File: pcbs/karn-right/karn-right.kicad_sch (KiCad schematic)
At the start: 45 parts, among them J1 S2B-PH-K-SLFSN, SW11 SW_Push, SW12 SW_Push, SW13 SW_Push, SW14 SW_Push, SW15 SW_Push, SW21 SW_Push, SW22 SW_Push, SW23 SW_Push, SW24 SW_Push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

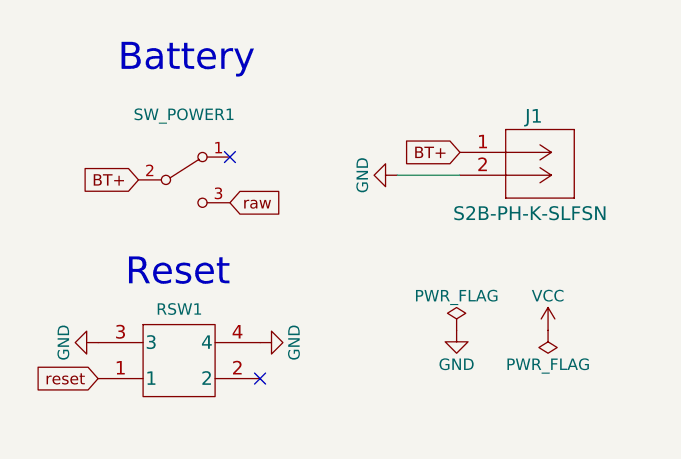
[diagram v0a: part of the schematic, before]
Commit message: Update karn-left pcb
- Apply various fixes from lessons learned on karn-right
- Fix incorrectly oriented reset switch
- Swap incorrect default polarity of JST connector footprint
- Increase size of diode pads
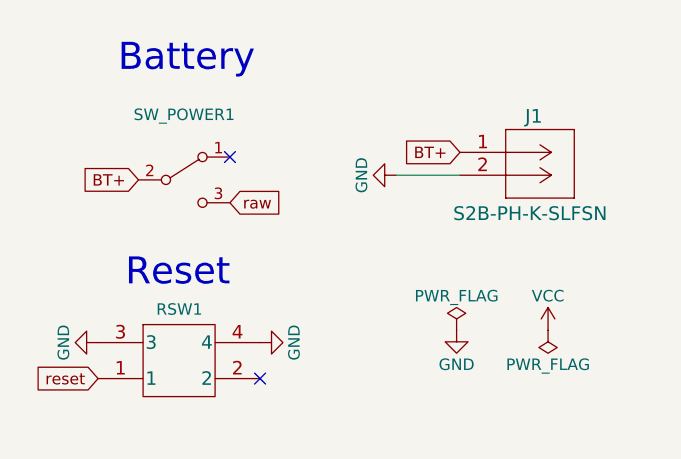
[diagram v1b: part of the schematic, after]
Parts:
- J1: footprint kbd:S2B-PH-K-SLFSN -> CONN_S2B-PH-K-S_JST; symbol S2B-PH-K-SLFSN:S2B-PH-K-SLFSN -> karn-symbols:battery-connector-S2B-PH-K-SLFSN
- RSW1: footprint TL3313AF250QG_EWI -> karn-kicad:reset-switch-TL3313AF250QG
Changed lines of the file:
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@@
+    (stroke (width 0) (type default) (color 0 0 0 0))
+  )
+  (wire (pts (xy 247.3957 68.2818) (xy 254.4891 68.2818))
     (stroke (width 0) (type default) (color 0 0 0 0))
   )
@@
   )
   (wire (pts (xy 34.5261 135.6582) (xy 37.5261 135.6582))
-    (stroke (width 0) (type default) (color 0 0 0 0))
-  )
-  (wire (pts (xy 247.4891 68.2818) (xy 254.4891 68.2818))
     (stroke (width 0) (type default) (color 0 0 0 0))
   )
@@
       (effects (font (size 1.27 1.27)) hide)
     )
-    (property "Footprint" "TL3313AF250QG_EWI" (id 2) (at 224.2785 94.8773 0)
+    (property "Footprint" "karn-kicad:reset-switch-TL3313AF250QG" (id 2) (at 224.2785 94.8773 0)
       (effects (font (size 1.524 1.524)) hide)
     )
@@
     (pin "2")
   )
-  (symbol (lib_id "power:GND") (at 247.4891 68.2818 270) (unit 1)
-    (in_bom yes) (on_board yes)
-    (property "Reference" "#PWR07" (id 0) (at 241.1391 68.2818 0)
-      (effects (font (size 1.27 1.27)) hide)
-    )
-    (property "Value" "GND" (id 1) (at 243.6791 68.2818 0))
-    (property "Footprint" "" (id 2) (at 247.4891 68.2818 0)
-      (effects (font (size 1.27 1.27)) hide)
-    )
-    (property "Datasheet" "" (id 3) (at 247.4891 68.2818 0)
-      (effects (font (size 1.27 1.27)) hide)
-    )
-    (pin "1")
-  )
-  (symbol (lib_id "S2B-PH-K-SLFSN:S2B-PH-K-SLFSN") (at 254.4891 65.7418 0) (unit 1)
+  (symbol (lib_id "power:GND") (at 247.3957 68.2818 270) (unit 1)
+    (in_bom yes) (on_board yes)
+    (property "Reference" "#PWR07" (id 0) (at 241.0457 68.2818 0)
+      (effects (font (size 1.27 1.27)) hide)
+    )
+    (property "Value" "GND" (id 1) (at 243.5857 68.2818 0))
+    (property "Footprint" "" (id 2) (at 247.3957 68.2818 0)
+      (effects (font (size 1.27 1.27)) hide)
+    )
+    (property "Datasheet" "" (id 3) (at 247.3957 68.2818 0)
+      (effects (font (size 1.27 1.27)) hide)
+    )
+    (pin "1")
+  )
+  (symbol (lib_id "karn-symbols:battery-connector-S2B-PH-K-SLFSN") (at 254.4891 65.7418 0) (unit 1)
     (in_bom yes) (on_board yes)
     (property "Reference" "J1" (id 0) (at 261.7204 61.7418 0)
@@
       (effects (font (size 1.524 1.524)) (justify left))
     )
-    (property "Footprint" "kbd:S2B-PH-K-SLFSN" (id 2) (at 264.6491 67.2658 0)
+    (property "Footprint" "CONN_S2B-PH-K-S_JST" (id 2) (at 264.7391 72.9918 0)
       (effects (font (size 1.524 1.524)) hide)
     )
     (property "Datasheet" "" (id 3) (at 254.4891 65.7418 0)
-      (effects (font (size 1.524 1.524)) hide)
+      (effects (font (size 1.524 1.524)))
     )
     (pin "1")
@@
   (symbol (lib_id "power:GND") (at 214.2785 86.8773 270) (unit 1)
     (in_bom yes) (on_board yes)
-    (property "Reference" "#PWR?" (id 0) (at 207.9285 86.8773 0)
+    (property "Reference" "#PWR0101" (id 0) (at 207.9285 86.8773 0)
       (effects (font (size 1.27 1.27)) hide)
     )
@@
     )
     (path "/e3a47704-cb4a-4555-aa4f-d3ca75c136b6"
-      (reference "#PWR?") (unit 1) (value "GND") (footprint "")
+      (reference "#PWR0101") (unit 1) (value "GND") (footprint "")
     )
     (path "/817acd3d-65d5-4d98-84f9-5556e4094c7a"
@@
     )
     (path "/a53ef69a-8078-4623-9cd4-3672c42f5863"
-      (reference "J1") (unit 1) (value "S2B-PH-K-SLFSN") (footprint "kbd:S2B-PH-K-SLFSN")
+      (reference "J1") (unit 1) (value "S2B-PH-K-SLFSN") (footprint "CONN_S2B-PH-K-S_JST")
     )
     (path "/7f9c7077-7594-446f-ae61-381d3d9fb6cc"
@@
     )
     (path "/0eece0c9-6947-4883-a87e-b445b80630d9"
-      (reference "RSW1") (unit 1) (value "SW_Push") (footprint "TL3313AF250QG_EWI")
+      (reference "RSW1") (unit 1) (value "SW_Push") (footprint "karn-kicad:reset-switch-TL3313AF250QG")
     )
     (path "/60c85a9c-c0d2-4469-b84c-2eacd924bd6c"
